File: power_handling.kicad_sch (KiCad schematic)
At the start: 45 parts, among them U1 TPS62065DSGR, U2 TPS62130, U3 TPS62130, U4 TLV75518PDBVR

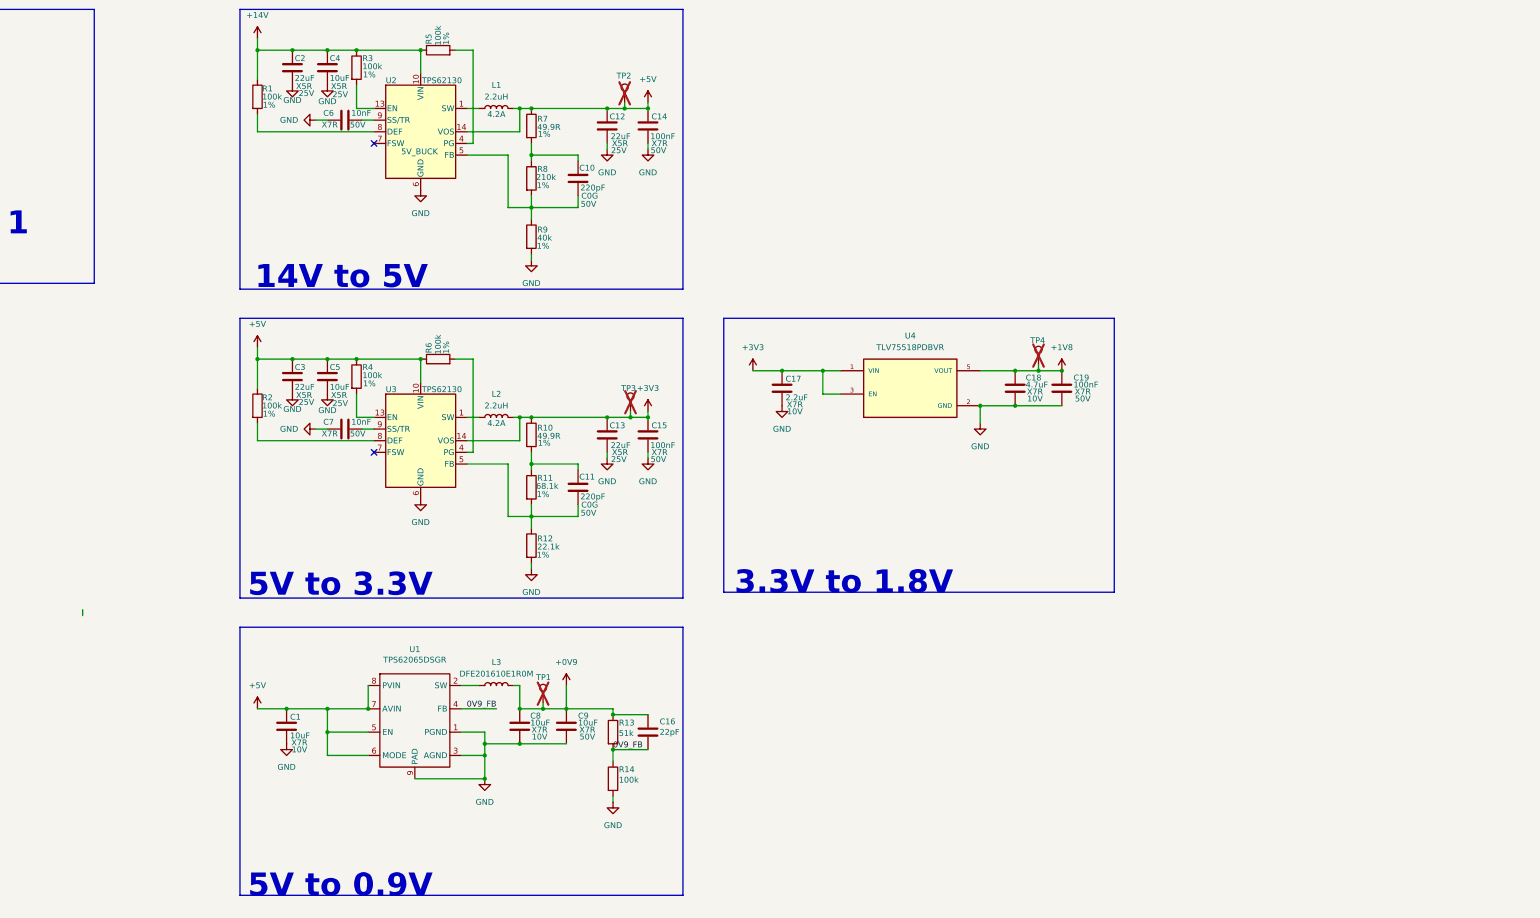
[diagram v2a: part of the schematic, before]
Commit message: Publish ESP32-P4 multi-sheet hardware redesign
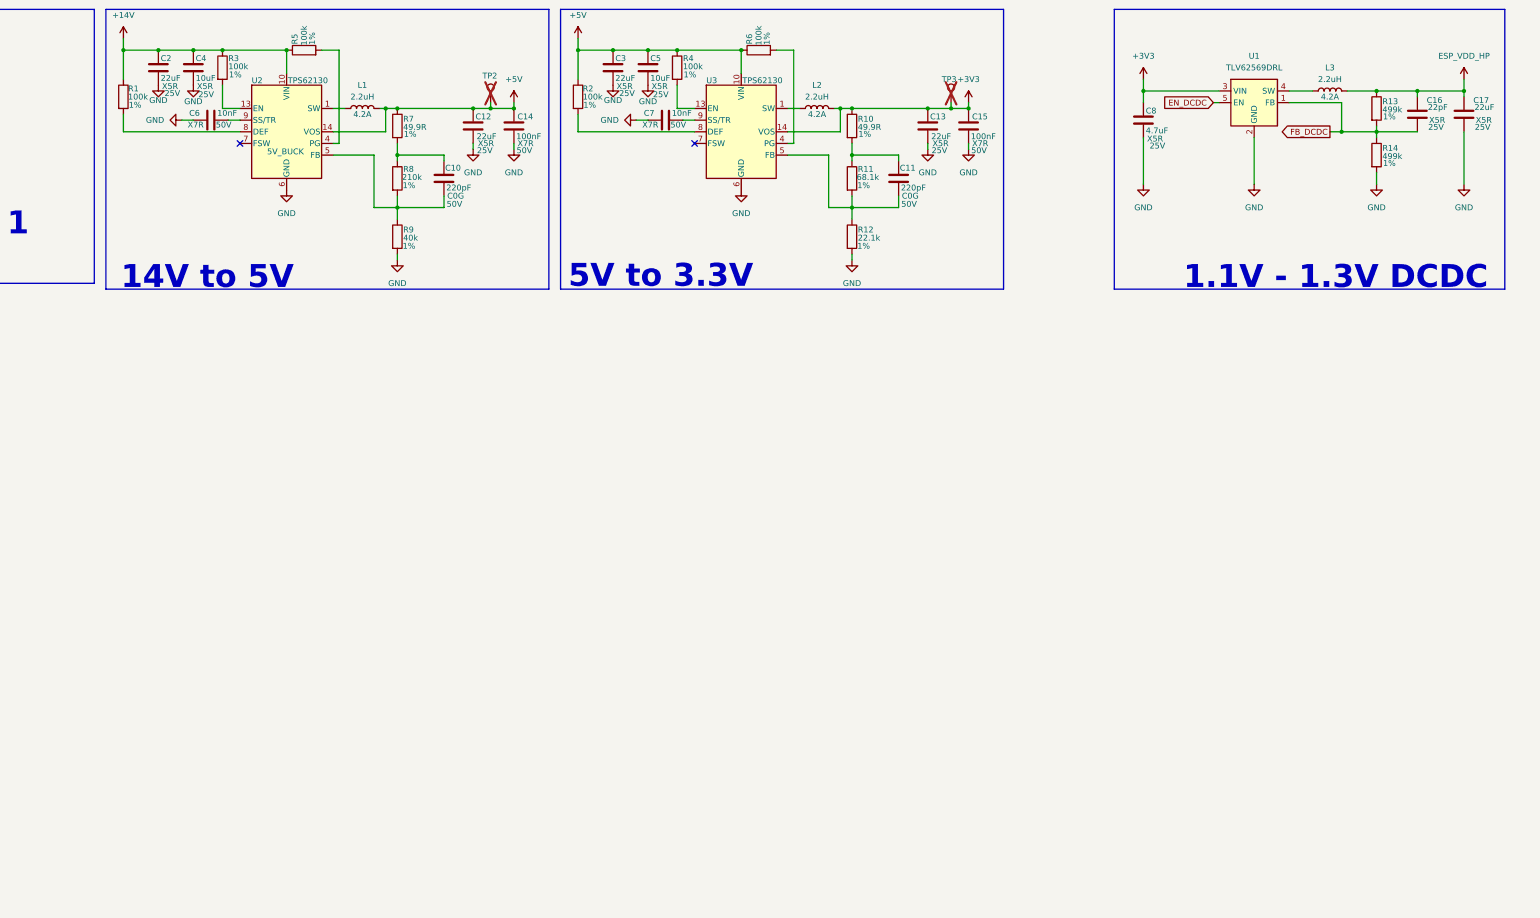
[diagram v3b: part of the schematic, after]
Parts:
- removed C1: 10uF, Capacitor_SMD:C_0603_1608Metric, symbol Device:C
- removed C18: 4.7uF, Capacitor_SMD:C_0603_1608Metric, symbol Device:C
- removed C19: 100nF, Capacitor_SMD:C_0805_2012Metric, symbol Device:C
- removed C9: 10uF, Capacitor_SMD:C_0805_2012Metric, symbol Device:C
- removed TP1, TP4: TestPoint, TestPoint:TestPoint_Pad_D1.0mm, symbol Connector:TestPoint
- removed U1: TPS62065DSGR, Ic:DFN8G-0.5-2X2MM, symbol New_Library:TPS62065DSGR
- removed U4: TLV75518PDBVR, Package_TO_SOT_SMD:SOT-23-5, symbol New_Library:MIC5365-1.8YC5-TR
- added U1: TLV62569DRL, Package_TO_SOT_SMD:SOT-563, symbol Regulator_Switching:TLV62569ADRL
- C16: Dielectric (none) -> X5R; Function 0.9V_BUCK_FEEDFORWARD -> 1.1V_BUCK; Manufacturer (none) -> Samsung Electro-Mechanics; Voltage (none) -> 25V
- C17: value 2.2uF -> 22uF; footprint Capacitor_SMD:C_0603_1608Metric -> Capacitor_SMD:C_0805_2012Metric; Dielectric X7R -> X5R; Function 1.8V_LDO -> 1.1V_BUCK; LCSC Part # C86018 -> C45783; Manufacturer Murata Electronics -> Samsung Electro-Mechanics; Manufacturer Part GRM188R71A225KE15D -> CL21A226MAQNNNE; Supplier Part C86018 -> C45783; Voltage 10V -> 25V
- C8: value 10uF -> 4.7uF; footprint Capacitor_SMD:C_0603_1608Metric -> Capacitor_SMD:C_0805_2012Metric; Dielectric X7R -> X5R; Function 0.9V_BUCK_OUT -> 1.1V_BUCK; LCSC Part # C913474 -> C45783; Manufacturer Murata Electronics -> Samsung Electro-Mechanics; Manufacturer Part GRM188Z71A475KE15D -> CL21A226MAQNNNE; Supplier Part C913474 -> C45783; Voltage 10V -> 25V
- L3: value DFE201610E1R0M -> 2.2uH; footprint Inductor_SMD:L_Murata_DFE201610P -> Inductor_SMD:L_Cenker_CKCS4020; Function 0.9V_BUCK -> 1.1V_BUCK; Isat 3.6A -> (none); LCSC Part # (none) -> C719179; MANUFACTURER Murata -> BOURNS; MF Murata -> (none); MP DFE201610E1R0M -> SRP4020TA-2R2M; Manufacturer Murata -> BOURNS; Manufacturer Part DFE201610E1R0M -> SRP4020TA-2R2M; Saturation (none) -> 4.2A; Supplier Part (none) -> C719179
- POWER_IN1: Function (none) -> POWER
- R13: value 51k -> 499k; footprint Resistor_SMD:R_0402_1005Metric -> Resistor_SMD:R_0603_1608Metric; Function 0.9V_BUCK_FB_TOP -> 1.1V_BUCK; Manufacturer (none) -> UNI-ROYAL(Uniroyal Elec); Tolerance (none) -> 1%
- R14: value 100k -> 499k; footprint Resistor_SMD:R_0402_1005Metric -> Resistor_SMD:R_0603_1608Metric; Function 0.9V_BUCK_FB_BOTTOM -> 1.1V_BUCK; Manufacturer (none) -> UNI-ROYAL(Uniroyal Elec); Tolerance (none) -> 1%
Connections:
- net +3V3: now also C8.1, U1.3 (VIN); no longer C17.1
- net GND: now also U1.2 (GND)
- net at L3.1: now also U1.4 (SW)
- net +0V9 renamed ESP_VDD_HP
- net ESP_VDD_HP: now also C17.1; no longer C8.1
- net 0V9_FB renamed FB_DCDC
- net FB_DCDC: now also U1.1 (FB)
- new net EN_DCDC: U1.5 (EN)
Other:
- note added: "1.1V - 1.3V DCDC"
- note removed: "3.3V to 1.8V"
- note removed: "5V to 0.9V"
- moved on the sheet: C10, C11, C12, C13, C14, C15, C2, C3, C4, C5, C6, C7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

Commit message: v3 hardware changes
Full redesing, ready for prototype order
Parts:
- removed R1, R2, R5, R6: 100k, Resistor_SMD:R_0402_1005Metric, symbol Device:R
- added D5: PMEG4030ER, Diode_SMD:Nexperia_CFP3_SOD-123W, symbol Diode:PMEG4030ER
- added TP4: GND, TestPoint:TestPoint_THTPad_D3.0mm_Drill1.5mm, symbol Connector:TestPoint
- TP2: value TestPoint -> +5V
- TP3: value TestPoint -> +3V3
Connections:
- net +14V: now also D5.1 (K); no longer POWER_IN1.10, POWER_IN1.7, POWER_IN1.8, POWER_IN1.9
- net GND: now also U2.8 (DEF), U3.8 (DEF), TP4.1
- new net: D5.2 (A), POWER_IN1.10, POWER_IN1.7, POWER_IN1.8, POWER_IN1.9
- no-connect marks 2 -> 4
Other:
- moved on the sheet: C10, C11, C12, C13, C14, C15, C16, C17, C2, C3, C4, C5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

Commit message: v3 hardware ready for prototyping
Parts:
- C16: Dielectric X5R -> C0G; LCSC Part # (none) -> C1555; Manufacturer Samsung Electro-Mechanics -> FH; Manufacturer Part (none) -> 0402CG220J500NT; Supplier Part (none) -> C1555; Voltage 25V -> 50V
- C8: LCSC Part # C45783 -> C1779; Manufacturer Part CL21A226MAQNNNE -> CL21A475KAQNNNE; Supplier Part C45783 -> C1779
- D5: Function (none) -> POWER; LCSC Part # (none) -> C389355; Manufacturer (none) -> Nexperia; Manufacturer Part (none) -> PMEG4030ER,115; Supplier Part (none) -> C389355
- R13, R14: LCSC Part # (none) -> C2828669; Manufacturer UNI-ROYAL(Uniroyal Elec) -> Viking; Manufacturer Part (none) -> ARG03DTC4993; Supplier Part (none) -> C2828669
- R3, R4: LCSC Part # C25530 -> C25741; Manufacturer Part 0402WGJ0104TCE -> 0402WGF1003TCE; Supplier Part C25530 -> C25741
- R9: value 40k -> 40.2k; LCSC Part # C3016445 -> C12447; Manufacturer VO -> UNI-ROYAL; Manufacturer Part SCR0603F40K -> 0603WAF4022T5E; Supplier Part C3016445 -> C12447
- U1: value TLV62569DRL -> TLV62569DRLR; Manufacturer (none) -> Texas Instruments; Manufacturer Part (none) -> TLV62569DRLR
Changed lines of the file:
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@@
 	(title_block
 		(title "Drop in replacement PCB for Nest mini GEN2")
-		(rev "v1")
+		(date "2026-10-31")
+		(rev "v3")
 		(company "by iMike78 (inpired by Onju voice and HA VPE)")
 	)
@@
 			)
 		)
-		(property "Value" "40k"
+		(property "Value" "40.2k"
 			(at 78.74 125.984 0)
 			(show_name no)
@@
 			)
 		)
-		(property "Supplier Part" "C3016445"
+		(property "Supplier Part" "C12447"
 			(at 77.47 125.73 0)
 			(hide yes)
@@
 			)
 		)
-		(property "Manufacturer" "VO"
+		(property "Manufacturer" "UNI-ROYAL"
 			(at 77.47 125.73 0)
 			(hide yes)
@@
 			)
 		)
-		(property "Manufacturer Part" "SCR0603F40K"
+		(property "Manufacturer Part" "0603WAF4022T5E"
 			(at 77.47 125.73 0)
 			(hide yes)
@@
 			)
 		)
-		(property "LCSC Part #" "C3016445"
+		(property "LCSC Part #" "C12447"
 			(at 77.47 125.73 0)
 			(hide yes)
@@
 			)
 		)
-		(property "Dielectric" "X5R"
+		(property "Dielectric" "C0G"
 			(at 222.758 101.6 0)
 			(show_name no)
@@
 			)
 		)
-		(property "Voltage" "25V"
+		(property "Voltage" "50V"
 			(at 222.504 103.124 0)
 			(show_name no)
@@
 			)
 		)
-		(property "Supplier Part" ""
+		(property "Supplier Part" "C1555"
 			(at 218.44 100.33 0)
 			(hide yes)
@@
 			)
 		)
-		(property "Manufacturer" "Samsung Electro-Mechanics"
+		(property "Manufacturer" "FH"
 			(at 218.44 100.33 0)
 			(hide yes)
@@
 			)
 		)
-		(property "Manufacturer Part" ""
+		(property "Manufacturer Part" "0402CG220J500NT"
 			(at 218.44 100.33 0)
 			(hide yes)
@@
 			)
 		)
-		(property "LCSC Part #" ""
+		(property "LCSC Part #" "C1555"
 			(at 218.44 100.33 0)
 			(hide yes)
@@
 			)
 		)
-		(property "Supplier Part" "C45783"
+		(property "Supplier Part" "C1779"
 			(at 158.75 101.6 0)
 			(hide yes)
@@
 			)
 		)
-		(property "Manufacturer Part" "CL21A226MAQNNNE"
+		(property "Manufacturer Part" "CL21A475KAQNNNE"
 			(at 158.75 101.6 0)
 			(hide yes)
@@
 			)
 		)
-		(property "LCSC Part #" "C45783"
+		(property "LCSC Part #" "C1779"
 			(at 158.75 101.6 0)
 			(hide yes)
@@
 			)
 		)
-		(property "Supplier Part" ""
+		(property "Supplier Part" "C2828669"
 			(at 209.55 109.22 0)
 			(hide yes)
@@
 			)
 		)
-		(property "Manufacturer" "UNI-ROYAL(Uniroyal Elec)"
+		(property "Manufacturer" "Viking"
 			(at 209.55 109.22 0)
 			(hide yes)
@@
 			)
 		)
-		(property "Manufacturer Part" ""
+		(property "Manufacturer Part" "ARG03DTC4993"
 			(at 209.55 109.22 0)
 			(hide yes)
@@
 			)
 		)
-		(property "LCSC Part #" ""
+		(property "LCSC Part #" "C2828669"
 			(at 209.55 109.22 0)
 			(hide yes)
@@
 			)
 		)
-		(property "Supplier Part" ""
+		(property "Supplier Part" "C2828669"
 			(at 209.55 99.06 0)
 			(hide yes)
@@
 			)
 		)
-		(property "Manufacturer" "UNI-ROYAL(Uniroyal Elec)"
+		(property "Manufacturer" "Viking"
 			(at 209.55 99.06 0)
 			(hide yes)
@@
 			)
 		)
-		(property "Manufacturer Part" ""
+		(property "Manufacturer Part" "ARG03DTC4993"
 			(at 209.55 99.06 0)
 			(hide yes)
@@
 			)
 		)
-		(property "LCSC Part #" ""
+		(property "LCSC Part #" "C2828669"
 			(at 209.55 99.06 0)
 			(hide yes)
@@
 			)
 		)
+		(property "Function" "POWER"
+			(at 63.5 48.26 0)
+			(hide yes)
+			(show_name no)
+			(do_not_autoplace no)
+			(effects
+				(font
+					(size 1.27 1.27)
+				)
+			)
+		)
+		(property "LCSC Part #" "C389355"
+			(at 63.5 48.26 0)
+			(hide yes)
+			(show_name no)
+			(do_not_autoplace no)
+			(effects
+				(font
+					(size 1.27 1.27)
+				)
+			)
+		)
+		(property "Manufacturer" "Nexperia"
+			(at 63.5 48.26 0)
+			(hide yes)
+			(show_name no)
+			(do_not_autoplace no)
+			(effects
+				(font
+					(size 1.27 1.27)
+				)
+			)
+		)
+		(property "Manufacturer Part" "PMEG4030ER,115"
+			(at 63.5 48.26 0)
+			(hide yes)
+			(show_name no)
+			(do_not_autoplace no)
+			(effects
+				(font
+					(size 1.27 1.27)
+				)
+			)
+		)
+		(property "Supplier Part" "C389355"
+			(at 63.5 48.26 0)
+			(hide yes)
+			(show_name no)
+			(do_not_autoplace no)
+			(effects
+				(font
+					(size 1.27 1.27)
+				)
+			)
+		)
 		(pin "2"
 		)
@@
 			)
 		)
-		(property "Value" "TLV62569DRL"
+		(property "Value" "TLV62569DRLR"
 			(at 182.88 90.17 0)
 			(show_name no)
@@
 			)
 		)
+		(property "Manufacturer" "Texas Instruments"
+			(at 182.88 97.79 0)
+			(hide yes)
+			(show_name no)
+			(do_not_autoplace no)
+			(effects
+				(font
+					(size 1.27 1.27)
+				)
+			)
+		)
+		(property "Manufacturer Part" "TLV62569DRLR"
+			(at 182.88 97.79 0)
+			(hide yes)
+			(show_name no)
+			(do_not_autoplace no)
+			(effects
+				(font
+					(size 1.27 1.27)
+				)
+			)
+		)
 		(pin "4"
 		)
@@
 			)
 		)
-		(property "Supplier Part" "C25530"
+		(property "Supplier Part" "C25741"
 			(at 177.8 26.67 0)
 			(hide yes)
@@
 			)
 		)
-		(property "Manufacturer Part" "0402WGJ0104TCE"
+		(property "Manufacturer Part" "0402WGF1003TCE"
 			(at 177.8 26.67 0)
 			(hide yes)
@@
 			)
 		)
-		(property "LCSC Part #" "C25530"
+		(property "LCSC Part #" "C25741"
 			(at 177.8 26.67 0)
 			(hide yes)
@@
 			)
 		)
-		(property "Supplier Part" "C25530"
+		(property "Supplier Part" "C25741"
 			(at 39.37 88.9 0)
 			(hide yes)
@@
 			)
 		)
-		(property "Manufacturer Part" "0402WGJ0104TCE"
+		(property "Manufacturer Part" "0402WGF1003TCE"
 			(at 39.37 88.9 0)
 			(hide yes)
@@
 			)
 		)
-		(property "LCSC Part #" "C25530"
+		(property "LCSC Part #" "C25741"
 			(at 39.37 88.9 0)
 			(hide yes)
